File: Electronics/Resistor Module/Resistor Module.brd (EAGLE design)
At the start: 50 x 50 mm, 110 parts, among them IC1 74HC595D, IC2 74HC595D, IC3 74HC595D, IC4 74HC595D

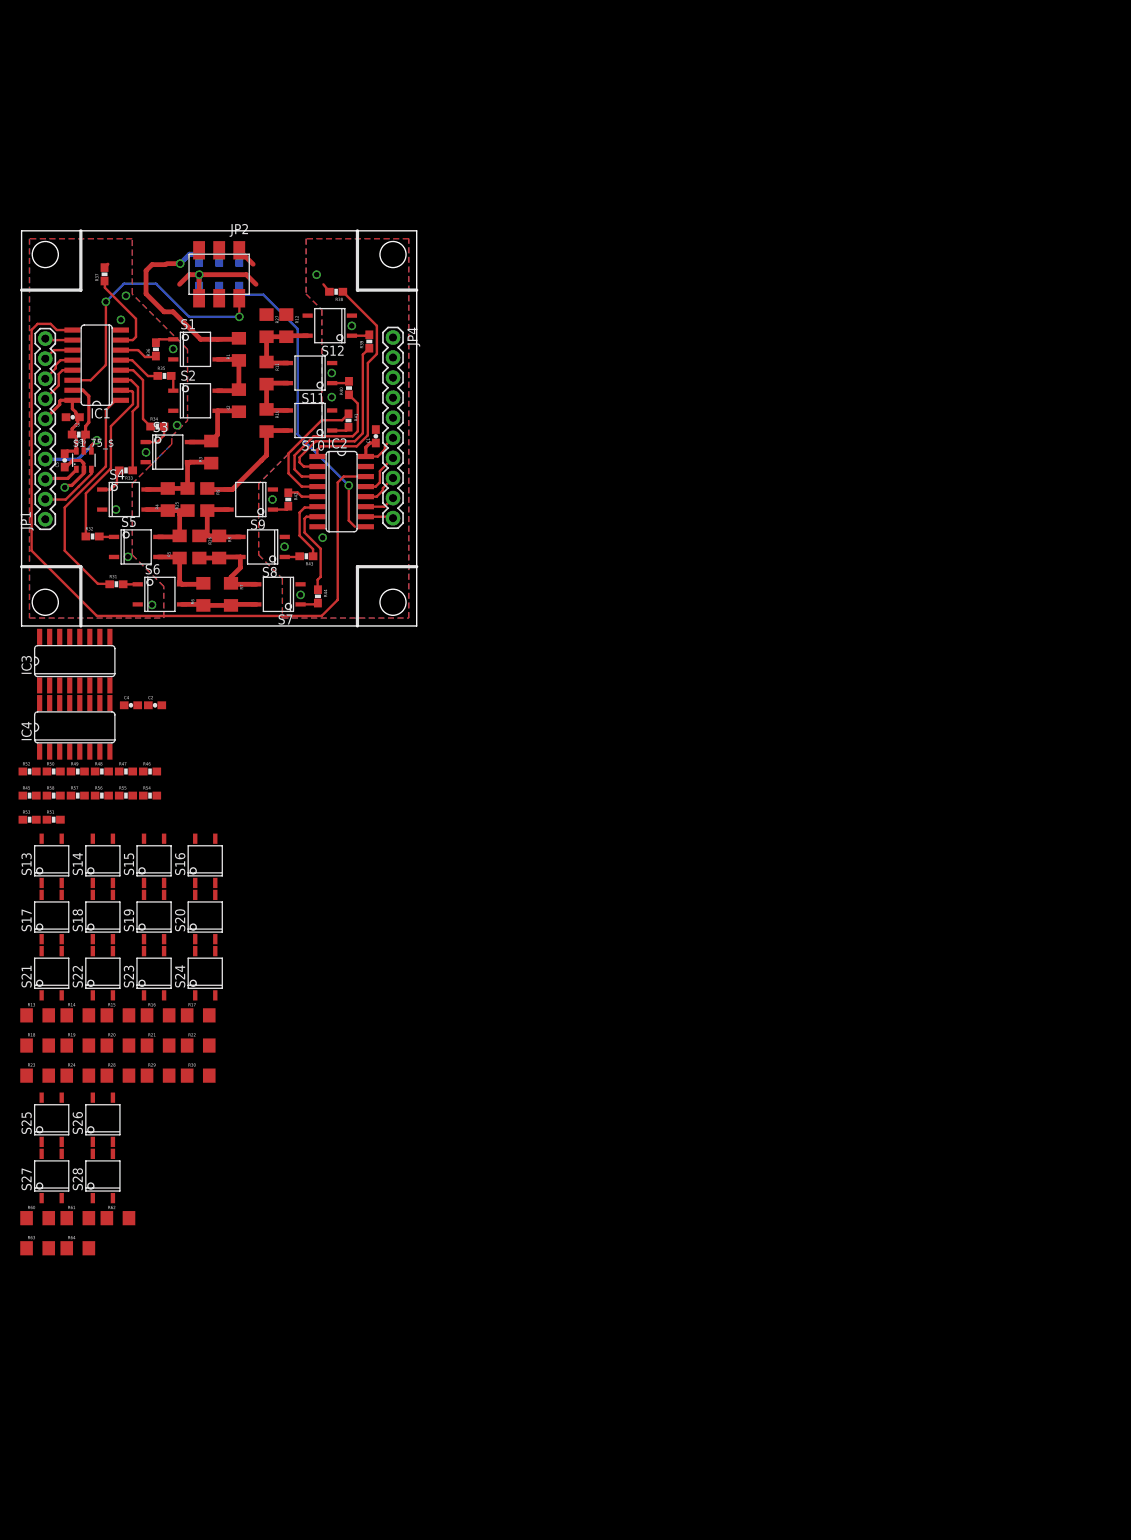
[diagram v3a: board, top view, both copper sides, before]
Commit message: Updated schematic for full range module. 1/4 layout done.
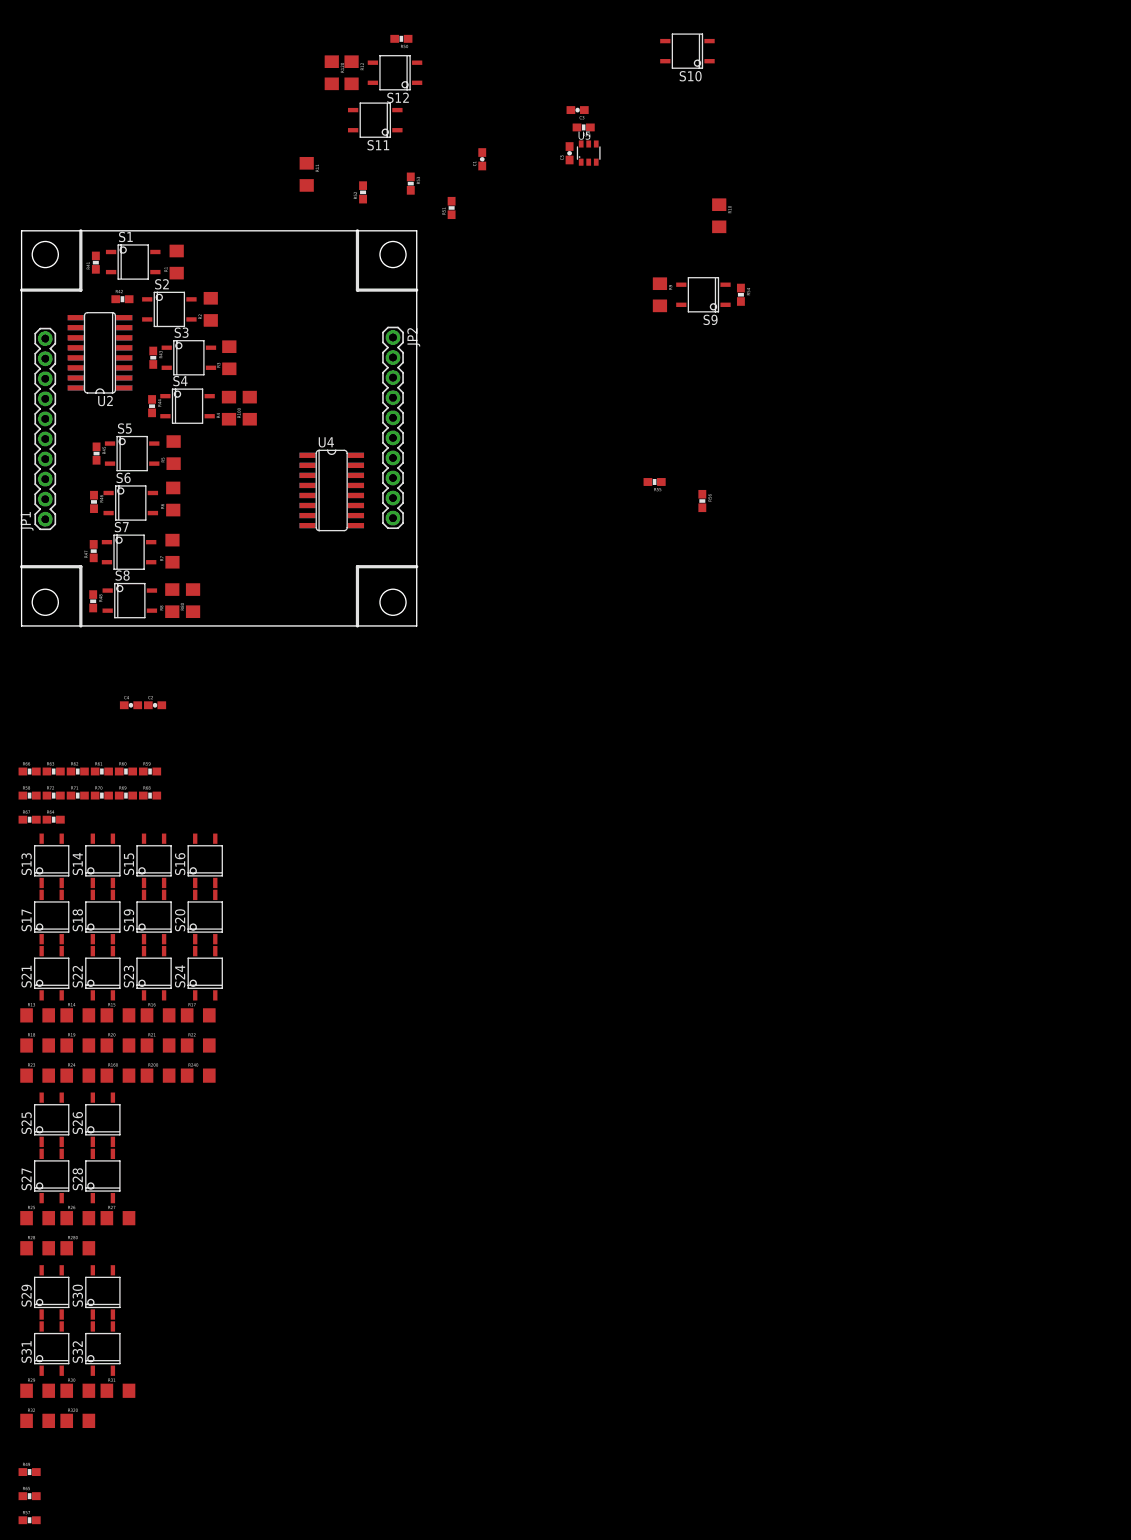
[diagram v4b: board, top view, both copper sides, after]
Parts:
- removed $1_75_$: 25AA010A, Resistor Module Library:SOT23-6
- removed IC1, IC2, IC3, IC4: 74HC595D, Resistor Module Library:SO16
- removed JP3: (no value), Resistor Module Library:2X3_SMT-M0.1
- removed JP4: M10PASSTHROUGH, Resistor Module Library:U4CON_18688_10
- removed R33, R34, R35, R36, R37, R38, R39, R40: 2k, Resistor Module Library:0603-RES
- added R100: 10, Resistor Module Library:1206
- added R120: 1k, Resistor Module Library:1206
- added R160: 10k, Resistor Module Library:1206
- added R200: 100k, Resistor Module Library:1206
- added R240: 1M, Resistor Module Library:1206
- added R280: 10M, Resistor Module Library:1206
- added R320: 100M, Resistor Module Library:1206
- added R65, R66, R67, R68, R69, R70, R71, R72: 2k, Resistor Module Library:0603-RES
- added R73: 10k, Resistor Module Library:0603-RES
- added R80: 100, Resistor Module Library:1206
- added S29, S30, S31, S32: CPC1002N, Resistor Module Library:CPC1002N
- added U1, U2, U3, U4: 74HC595D, Resistor Module Library:SO16
- added U5: 25AA010A, Resistor Module Library:SOT23-6
- JP2: value (none) -> M10PASSTHROUGH; device Resistor Module Library:969973-3 -> Resistor Module Library:U4CON_18688_10
- R25: value 10 -> 1M
- R26: value 100 -> 2M
- R27: value 1k -> 2M
- R28: value 10k -> 10M
- R29: value 100k -> 10M
- R30: value 1M -> 20M
- R31: value 2k -> 20M; device Resistor Module Library:0603-RES -> Resistor Module Library:1206
- R32: value 2k -> 100M; device Resistor Module Library:0603-RES -> Resistor Module Library:1206
- R59: value 10k -> 2k
- R60: value 1M -> 2k; device Resistor Module Library:1206 -> Resistor Module Library:0603-RES
- R61, R62: value 2M -> 2k; device Resistor Module Library:1206 -> Resistor Module Library:0603-RES
- R63, R64: value 10M -> 2k; device Resistor Module Library:1206 -> Resistor Module Library:0603-RES
- moved R27 114.5 mm to (12.2, -74.9), turned to 0 degrees
- moved R32 112.1 mm to (2.03, -100.6)
- moved R50 102.6 mm to (48.1, 74.3), turned to 180 degrees
- moved R31 102.1 mm to (12.2, -96.8)
- moved R54 98.0 mm to (91.0, 41.9), turned to 270 degrees
- moved R53 93.8 mm to (49.2, 56.0), turned to 270 degrees
- moved R25 92.9 mm to (2.03, -74.9), turned to 0 degrees
- moved R51 92.3 mm to (54.4, 52.9), turned to 90 degrees
- moved R57 91.9 mm to (1.02, -113.2)
- moved R49 88.9 mm to (1.02, -107.1)
- moved R26 86.3 mm to (7.11, -74.9), turned to 0 degrees
- moved R56 84.6 mm to (86.1, 15.8), turned to 270 degrees
- moved R52 84.6 mm to (43.2, 54.9), turned to 90 degrees
- moved R55 77.8 mm to (80.1, 18.2), turned to 180 degrees
- moved C3 74.8 mm to (70.4, 65.3)
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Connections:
- removed net N$40: R12.1, R13.2, R27.1, S12.P3, S13.P4
- removed net N$43: R16.1, R17.2, R28.1, S16.P3, S17.P4
- removed net N$9: R26.1, R8.1, R9.2, S8.P3, S9.P4
- removed net RELAY_POST_SHORT: R37.2, R51.2
- removed net RELAY_PRE_SHORT: R38.2, R52.2
- removed net R_DOWNSTREAM_IN: JP2.1
- removed net R_DOWNSTREAM_OUT: JP3.1
- removed net R_UPSTREAM: JP2.6, JP3.2
- removed net SERIAL_OUT: JP3.6
- new net N$53: R28.1, R280.1, R29.2, S28.P3, S29.P4
- new net N$58: R29.1, R30.2, S29.P3, S30.P4
- new net N$59: R30.1, R31.2, S30.P3, S31.P4
- new net N$60: R31.1, R32.2, R320.2, S31.P3, S32.P4
- new net N$61: R49.1, U2.15
- new net N$62: R57.1, U3.15
- new net N$64: R65.1, U4.15
- new net R120: R12.1, R120.1, R13.2, S12.P3, S13.P4
- new net R160: R16.1, R160.1, R17.2, S16.P3, S17.P4
- new net R80: R8.1, R80.1, R9.2, S8.P3, S9.P4
- new net RELAY_R29: R69.2, S29.P1
- new net RELAY_R30: R70.2, S30.P1
- new net RELAY_R31: R71.2, S31.P1
- new net RELAY_R32: R72.2, S32.P1
- new net R_OUT: JP2.2, R32.1, R320.1, S32.P3
- net 5V: now also R73.2, U1.16, U3.16, U5.6; no longer $1_75_$.6, IC1.16, IC3.16, R59.2
- net 5V_2: now also JP2.6, U2.16, U4.16; no longer IC2.16, IC4.16, JP4.6
- net EEPROM_CS_L: now also JP1.1, R73.1, U5.5; no longer $1_75_$.5, IC1.15, IC3.15, R59.1
- net EEPROM_MISO: now also U5.4; no longer $1_75_$.4
- net EEPROM_MOSI: now also U5.3; no longer $1_75_$.3
- net EEPROM_SCK: now also U5.1; no longer $1_75_$.1
- net GND: now also S29.P2, S30.P2, S31.P2, S32.P2, U1.8, U3.8, U5.2; no longer $1_75_$.2, IC1.8, IC3.8
- net GND_2: now also JP2.5, U2.8, U4.8; no longer IC2.8, IC4.8, JP4.5
- net N$1: now also R48.1, U1.7; no longer IC1.7, R37.1
- net N$12: now also R46.1, U1.5; no longer IC1.5, R35.1
- net N$13: now also R45.1, U1.4; no longer IC1.4, R34.1
- net N$14: now also R44.1, U1.3; no longer IC1.3, R33.1
- net N$15: now also R120.2; no longer R27.2
- net N$16: now also R43.1, U1.2; no longer IC1.2, R32.1
- net N$17: now also R42.1, U1.1; no longer IC1.1, R31.1
- net N$18: now also R50.1, U2.1; no longer IC2.1, R38.1
- net N$19: now also R51.1, U2.2; no longer IC2.2, R39.1
- net N$2: now also R47.1, U1.6; no longer IC1.6, R36.1
- net N$20: now also R52.1, U2.3; no longer IC2.3, R40.1
- net N$21: now also R53.1, U2.4; no longer IC2.4, R41.1
- net N$22: now also R54.1, U2.5; no longer IC2.5, R42.1
- net N$23: now also R55.1, U2.6; no longer IC2.6, R43.1
- net N$24: now also R56.1, U2.7; no longer IC2.7, R44.1
- net N$26: now also R64.1, U3.7; no longer IC3.7, R51.1
- net N$27: now also R63.1, U3.6; no longer IC3.6, R50.1
- net N$28: now also R62.1, U3.5; no longer IC3.5, R49.1
- net N$29: now also R61.1, U3.4; no longer IC3.4, R48.1
- net N$30: now also R60.1, U3.3; no longer IC3.3, R47.1
- net N$31: now also R59.1, U3.2; no longer IC3.2, R46.1
- net N$32: now also R58.1, U3.1; no longer IC3.1, R45.1
- net N$33: now also R66.1, U4.1; no longer IC4.1, R52.1
- net N$34: now also R67.1, U4.2; no longer IC4.2, R53.1
- net N$35: now also R68.1, U4.3; no longer IC4.3, R54.1
- net N$36: now also R69.1, U4.4; no longer IC4.4, R55.1
- net N$37: now also R70.1, U4.5; no longer IC4.5, R56.1
- net N$38: now also R71.1, U4.6; no longer IC4.6, R57.1
- net N$39: now also R72.1, U4.7; no longer IC4.7, R58.1
- net N$4: now also R100.2; no longer R25.2
- net N$42: now also R160.2; no longer R28.2
- net N$46: now also R200.2; no longer R29.2
- net N$47: now also R200.1; no longer R29.1
- net N$5: now also R100.1; no longer R25.1
- net N$50: now also R240.2; no longer R30.2
- net N$52: now also R240.1, R25.2; no longer R30.1, R60.2
- net N$54: now also R25.1, R26.2; no longer R60.1, R61.2
- net N$55: now also R26.1, R27.2; no longer R61.1, R62.2
- net N$56: now also R27.1, R28.2, R280.2; no longer R62.1, R63.2, R64.2
- net N$57: now also R41.1, U1.15; no longer R63.1, R64.1, S28.P3
- net N$8: now also R80.2; no longer R26.2
- net RELAY_R1: now also R41.2; no longer R36.2, R50.2
- net RELAY_R10: now also R50.2; no longer R41.2, R55.2
- net RELAY_R11: now also R51.2; no longer R40.2, R54.2
- net RELAY_R12: now also R52.2; no longer R39.2, R53.2
- net RELAY_R13: now also R53.2
- net RELAY_R14: now also R54.2
- net RELAY_R15: now also R55.2
- net RELAY_R16: now also R56.2
- net RELAY_R17: now also R57.2
- net RELAY_R18: now also R58.2
- net RELAY_R19: now also R59.2
- net RELAY_R2: now also R42.2; no longer R35.2, R49.2
- net RELAY_R20: now also R60.2
- net RELAY_R21: now also R61.2
- net RELAY_R22: now also R62.2
- net RELAY_R23: now also R63.2
- net RELAY_R24: now also R64.2
- net RELAY_R25: now also R65.2
- net RELAY_R26: now also R66.2
- net RELAY_R27: now also R67.2
- net RELAY_R28: now also R68.2
- net RELAY_R3: now also R43.2; no longer R34.2, R48.2
- net RELAY_R4: now also R44.2; no longer R33.2, R47.2
- net RELAY_R5: now also R45.2; no longer R32.2, R46.2
- net RELAY_R6: now also R46.2; no longer R31.2, R45.2
- net RELAY_R7: now also R47.2; no longer R44.2, R58.2
- net RELAY_R8: now also R48.2; no longer R43.2, R57.2
- net RELAY_R9: now also R49.2; no longer R42.2, R56.2
- net R_IN: now also JP2.1
- net SERIAL_CLK: now also JP1.8, U1.11, U2.11; no longer IC1.11, IC3.11, JP1.9
- net SERIAL_CLK_2: now also JP2.8, U3.11, U4.11; no longer IC2.11, IC4.11, JP4.9
- net SERIAL_IN: now also JP2.4, U1.14; no longer IC1.14, JP2.2
- net SERIAL_LATCH: now also JP1.9, U1.12, U2.12; no longer IC1.12, IC3.12, JP1.8
- net SERIAL_LATCH_2: now also JP2.9, U3.12, U4.12; no longer IC2.12, IC4.12, JP4.8
- net SERIAL_MR_L: now also JP1.7, U1.10, U2.10; no longer IC1.10, IC3.10, JP1.10
- net SERIAL_MR_L_2: now also JP2.7, U3.10, U4.10; no longer IC2.10, IC4.10, JP4.10
- net SERIAL_OE_L: now also JP1.10, U1.13, U2.13; no longer IC1.13, IC3.13, JP1.7
- net SERIAL_OE_L_2: now also JP2.10, U3.13, U4.13; no longer IC2.13, IC4.13, JP4.7
- net SERIAL_PASS: now also U1.9, U2.14; no longer IC1.9, IC2.14
- net SERIAL_PASS1: now also U2.9, U3.14; no longer IC2.9, IC3.14
- net SERIAL_PASS2: now also U3.9, U4.14; no longer IC3.9, IC4.14
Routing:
- net SERIAL_PASS: track 95.5 -> 0.00 mm
- net SERIAL_OUT: track 37.2 -> 0.00 mm, vias 1 -> 0
- net SERIAL_IN: track 35.0 -> 0.00 mm, vias 2 -> 0
- net N$17: track 29.8 -> 0.00 mm
- net N$18: track 28.4 -> 0.00 mm
- net N$19: track 23.5 -> 0.00 mm
- net N$16: track 22.4 -> 0.00 mm
- net R_IN: track 19.9 -> 0.00 mm
- net N$20: track 19.4 -> 0.00 mm
- net N$21: track 16.5 -> 0.00 mm
- net R_UPSTREAM: track 16.2 -> 0.00 mm, vias 1 -> 0
- net N$10: track 15.1 -> 0.00 mm
- net 5V: track 13.8 -> 0.00 mm
- net N$14: track 13.4 -> 0.00 mm
- net N$8: track 12.3 -> 0.00 mm
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- removed copper zone on layer 1, net GND
- removed copper zone on layer 16, net GND
- removed copper zone on layer 1, net GND_2
- removed copper zone on layer 16, net GND_2

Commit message: Placed another 1/4 of the board. Top layer preliminary completed
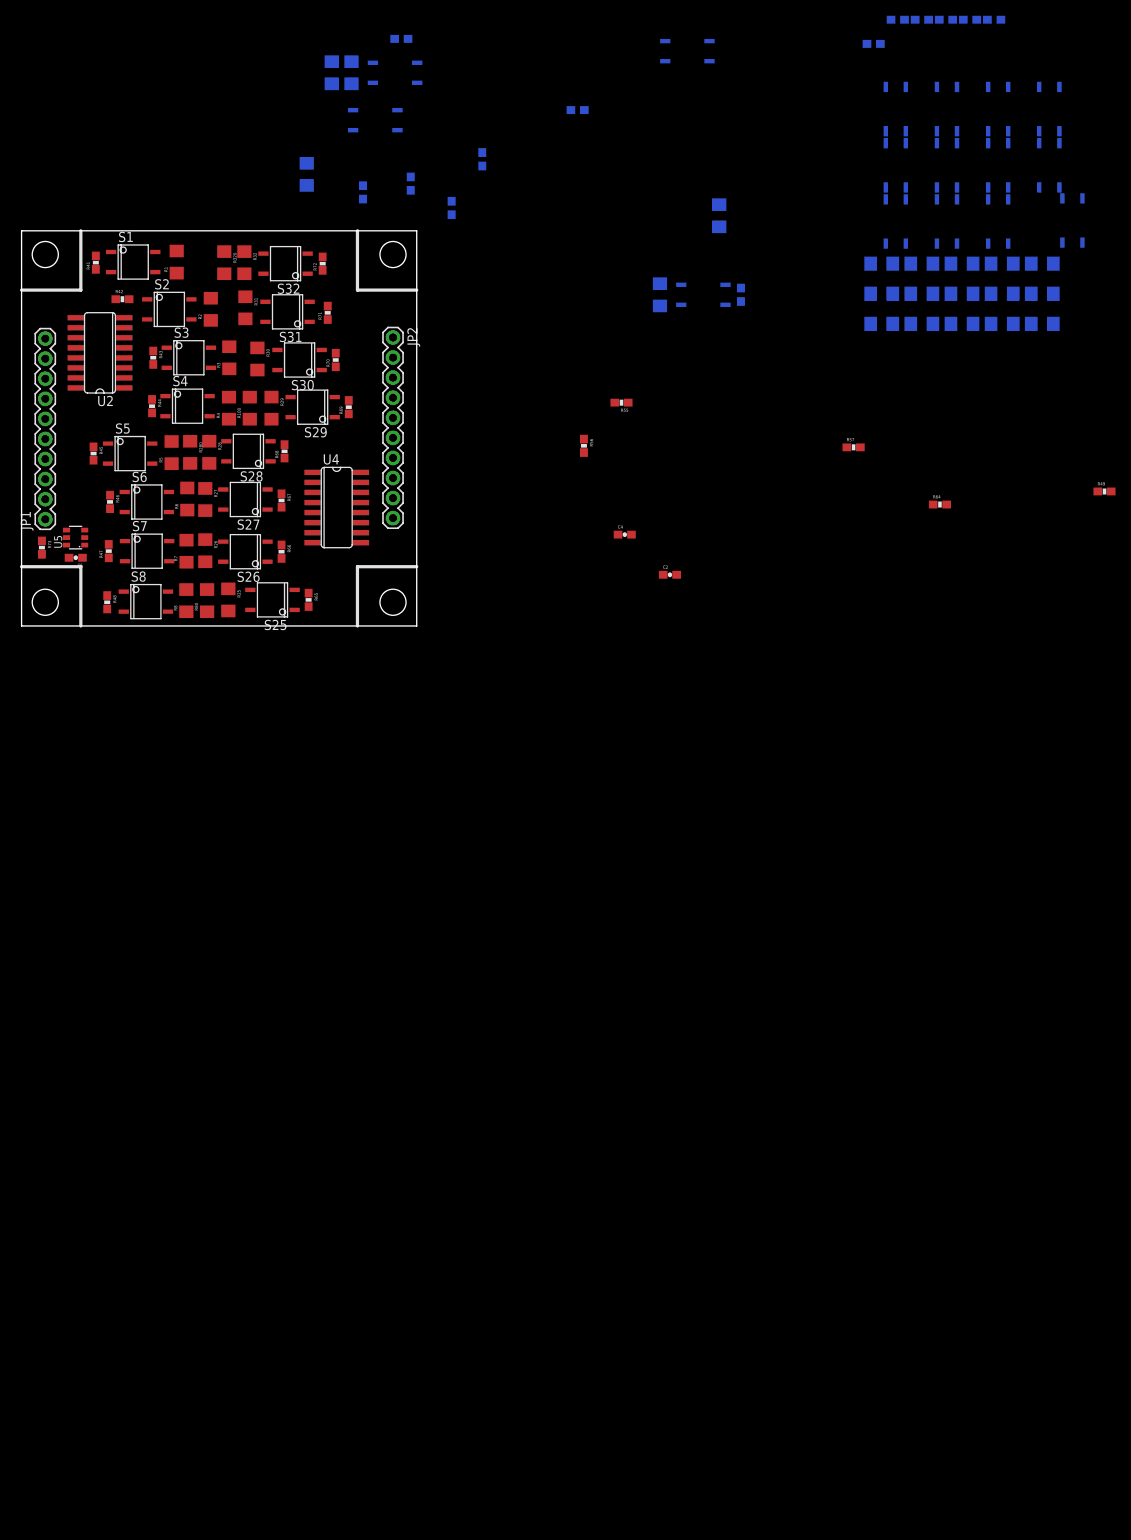
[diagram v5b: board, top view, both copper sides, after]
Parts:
- moved R49 184.1 mm to (137.0, 17.0)
- moved R57 171.2 mm to (105.3, 22.6)
- moved R32 148.9 mm to (28.2, 46.0), turned to 270 degrees
- moved R320 147.7 mm to (25.7, 46.0), turned to 270 degrees
- moved S24 145.3 mm to (133.0, 51.3), flipped to the bottom
- moved R13 143.0 mm to (108.8, 45.8), flipped to the bottom
- moved R14 143.0 mm to (113.9, 45.8), flipped to the bottom
- moved R15 143.0 mm to (119.0, 45.8), flipped to the bottom
- moved R16 143.0 mm to (124.1, 45.8), flipped to the bottom
- moved R17 143.0 mm to (129.2, 45.8), flipped to the bottom
- moved R18 143.0 mm to (108.8, 42.0), flipped to the bottom
- moved R19 143.0 mm to (113.9, 42.0), flipped to the bottom
- moved R23 143.0 mm to (108.8, 38.2), flipped to the bottom
- moved R24 143.0 mm to (113.9, 38.2), flipped to the bottom
- moved R59 143.0 mm to (123.1, 76.7), flipped to the bottom
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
